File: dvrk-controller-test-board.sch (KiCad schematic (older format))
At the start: 21 parts

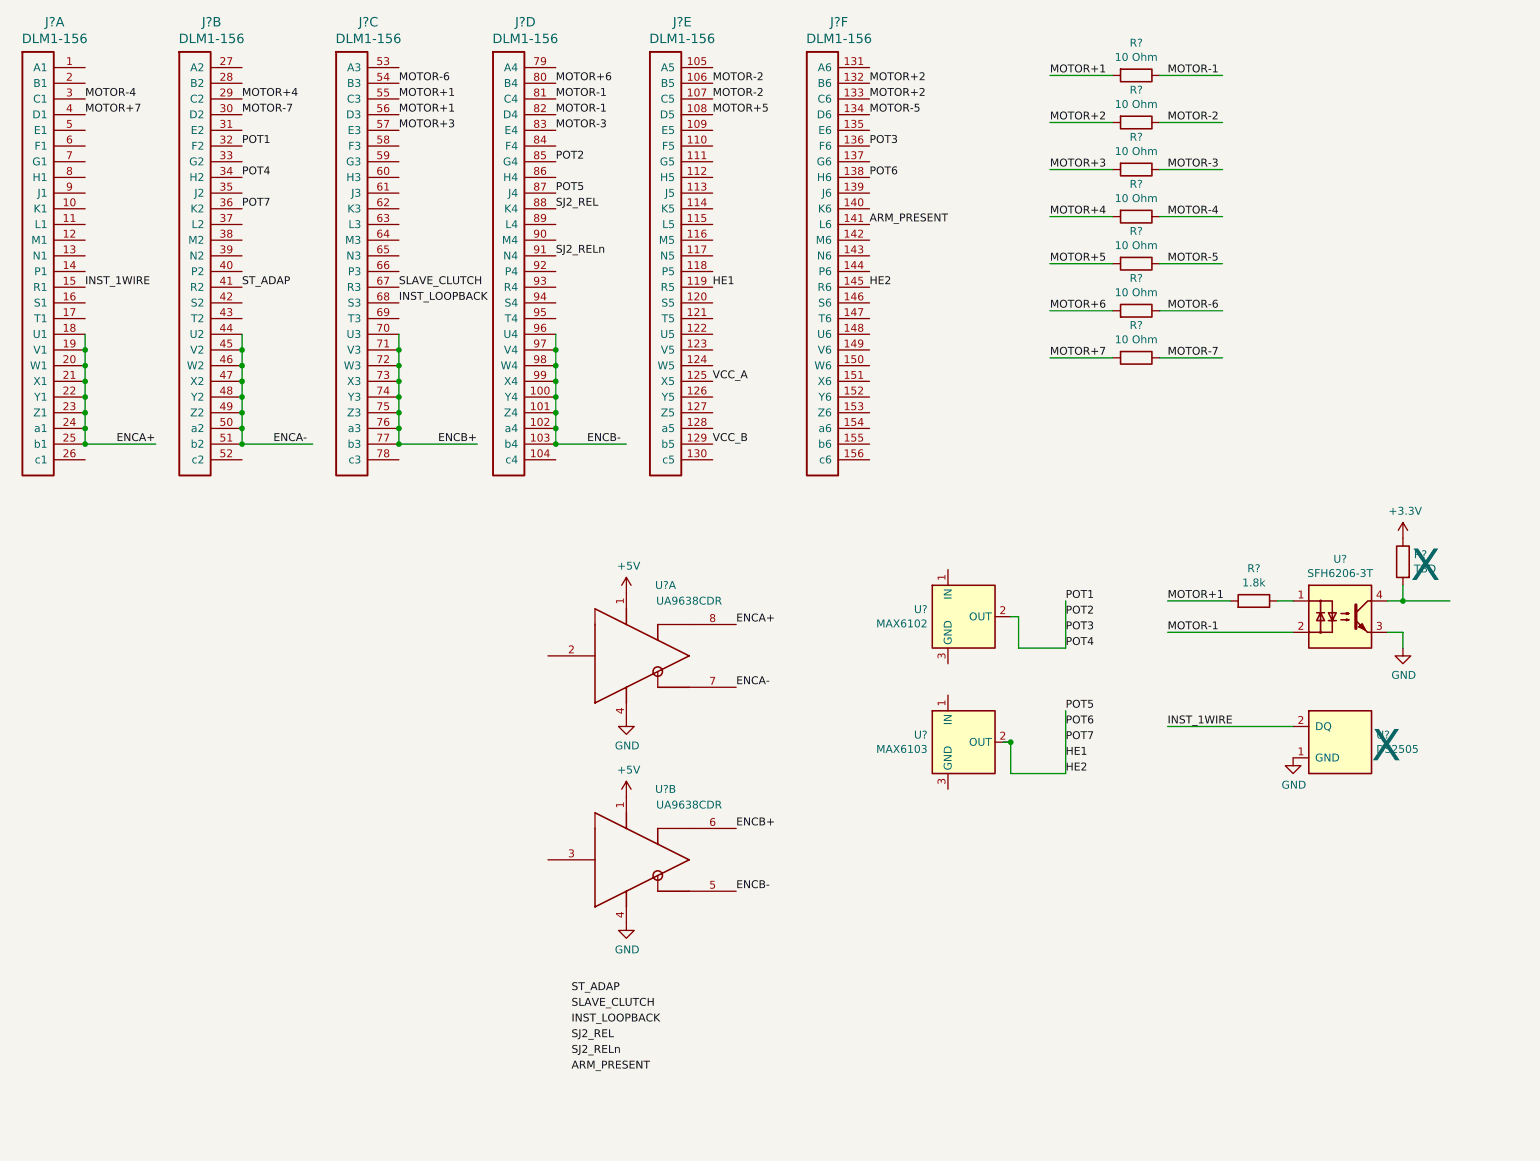
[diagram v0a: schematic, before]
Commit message: routing done. drc pass
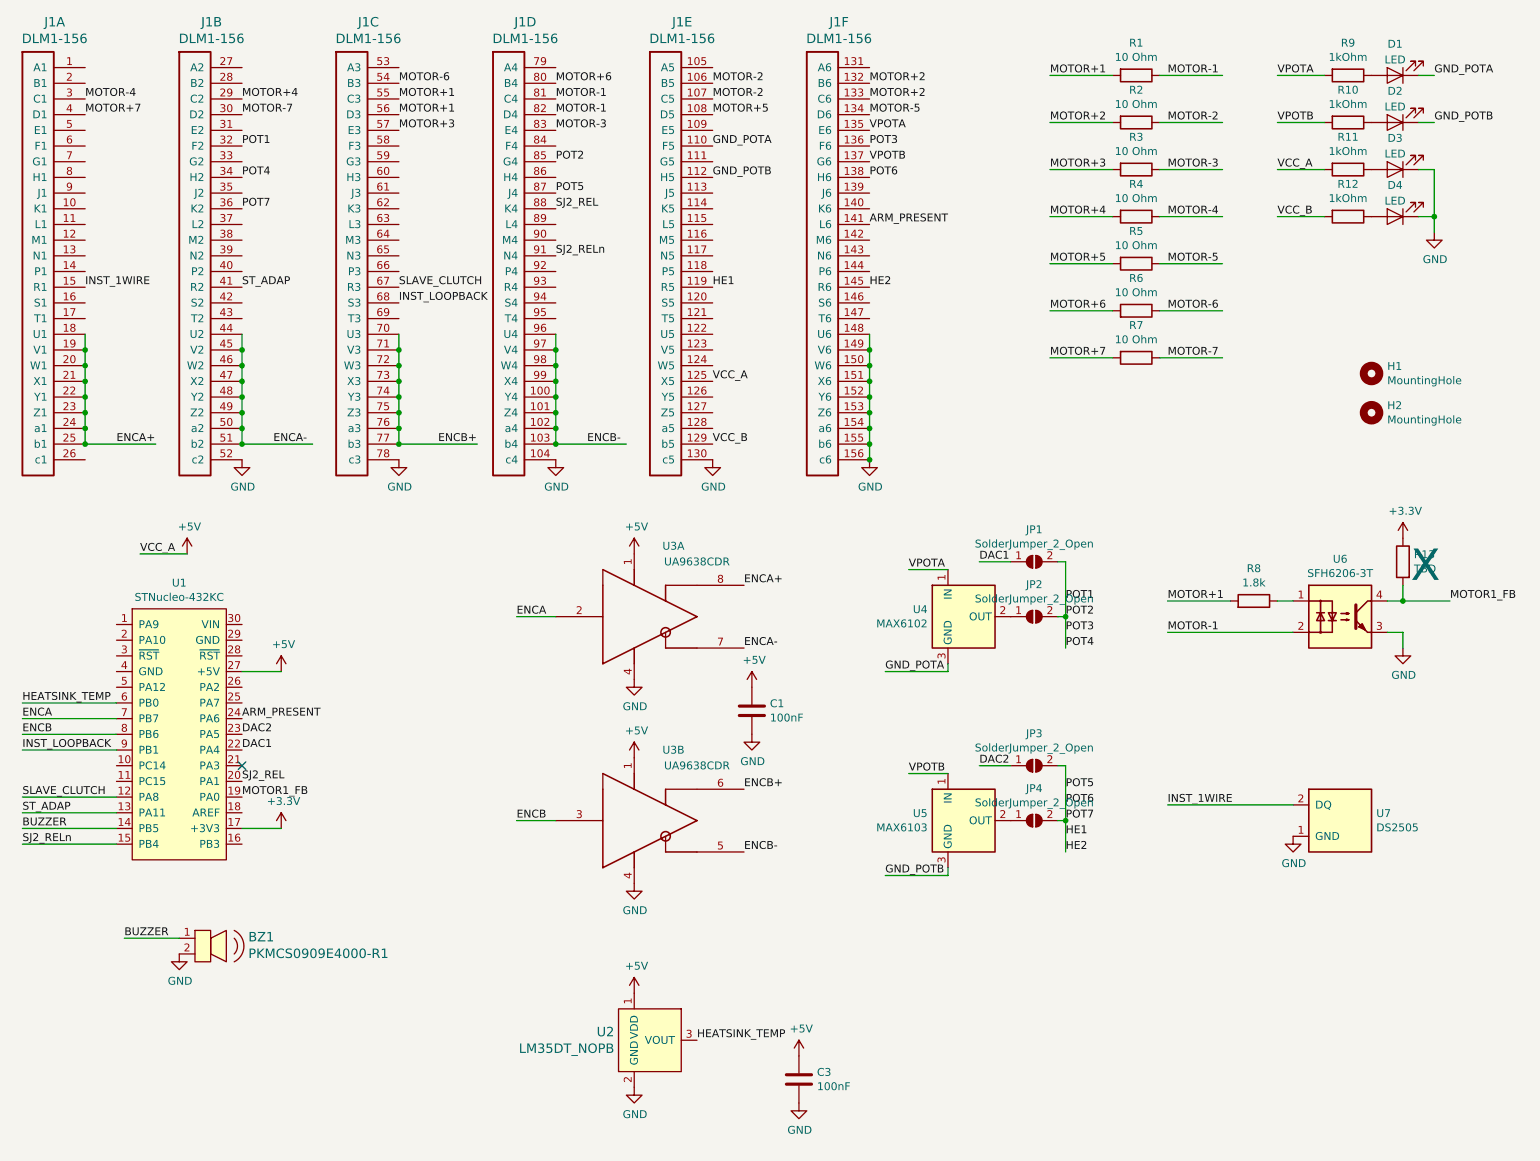
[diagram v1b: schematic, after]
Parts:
- added BZ1: PKMCS0909E4000-R1, digikey-footprints:Piezo_9x9mm_PKMCS0909E4000-R1, symbol dk_Alarms-Buzzers-and-Sirens:PKMCS0909E4000-R1
- added C1, C3: 100nF, Capacitor_SMD:C_0402_1005Metric, symbol Device:C
- added D1, D2, D3, D4: LED, LED_SMD:LED_0402_1005Metric, symbol Device:LED
- added H1, H2: MountingHole, MountingHole:MountingHole_3.2mm_M3, symbol Mechanical:MountingHole
- added JP1, JP2, JP3, JP4: SolderJumper_2_Open, Jumper:SolderJumper-2_P1.3mm_Open_TrianglePad1.0x1.5mm, symbol Jumper:SolderJumper_2_Open
- added R10, R11, R12, R9: 1kOhm, Resistor_SMD:R_0402_1005Metric, symbol Device:R
- added U1: STNucleo-432KC, dvrk:STNucleo32, symbol dvrk:STNucleo-432KC
- added U2: LM35DT_NOPB, Package_TO_SOT_THT:TO-220-3_Vertical, symbol dk_Temperature-Sensors-Analog-and-Digital-Output:LM35DT_NOPB
- J1: renamed from J?; footprint (none) -> dvrk:DLM1-Plug
- R1, R2, R3, R4, R5, R6, R7: renamed from R?; footprint (none) -> Package_TO_SOT_THT:TO-220-2_Vertical
- R13, R8: renamed from R?; footprint (none) -> Resistor_SMD:R_0402_1005Metric
- U7: renamed from U?; footprint (none) -> dvrk:TSOC-6
- gave numbers to parts that had none: 4
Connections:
- net labels added: BUZZER, DAC1, DAC2, ENCA, ENCB, GND_POTA, GND_POTB, HEATSINK_TEMP, MOTOR1_FB, VPOTA, VPOTB
- wire segments 63 -> 103
- no-connect marks 0 -> 1
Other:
- moved on the sheet: U3A, U3B, U5, U7

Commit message: added logo
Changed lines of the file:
@@
+	1    0    0    -1
+$EndComp
+$Comp
+L dvrk-logo:LOGO #G?
+U 1 1 5C5392A2
+P 6550 7050
+F 0 "#G?" H 6550 6947 60  0001 C CNN
+F 1 "LOGO" H 6550 7153 60  0001 C CNN
+F 2 "dvrk:dvrk-logo" H 6550 7050 50  0001 C CNN
+F 3 "" H 6550 7050 50  0001 C CNN
+	1    6550 7050
 	1    0    0    -1
 $EndComp

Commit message: reannotate
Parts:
- renumbered C3 to C2
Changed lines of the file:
@@
 	9100 4700 8300 4700
 $Comp
-L power:GND #PWR0101
+L power:GND #PWR022
 U 1 1 5C3598A0
 P 9800 4800
-F 0 "#PWR0101" H 9800 4550 50  0001 C CNN
+F 0 "#PWR022" H 9800 4550 50  0001 C CNN
 F 1 "GND" H 9805 4627 50  0000 C CNN
 F 2 "" H 9800 4800 50  0001 C CNN
@@
 	9800 4500 9800 4400
 $Comp
-L power:+3.3V #PWR0102
+L power:+3.3V #PWR021
 U 1 1 5C360C60
 P 9800 4100
-F 0 "#PWR0102" H 9800 3950 50  0001 C CNN
+F 0 "#PWR021" H 9800 3950 50  0001 C CNN
 F 1 "+3.3V" H 9815 4273 50  0000 C CNN
 F 2 "" H 9800 4100 50  0001 C CNN
@@
 	9100 5800 8300 5800
 $Comp
-L power:GND #PWR0103
+L power:GND #PWR020
 U 1 1 5C3C0652
 P 9100 6000
-F 0 "#PWR0103" H 9100 5750 50  0001 C CNN
+F 0 "#PWR020" H 9100 5750 50  0001 C CNN
 F 1 "GND" H 9105 5827 50  0000 C CNN
 F 2 "" H 9100 6000 50  0001 C CNN
@@
 ENCB-
 $Comp
-L power:GND #PWR0104
+L power:GND #PWR09
 U 1 1 5C3F2BBE
 P 4900 5000
-F 0 "#PWR0104" H 4900 4750 50  0001 C CNN
+F 0 "#PWR09" H 4900 4750 50  0001 C CNN
 F 1 "GND" H 4905 4827 50  0000 C CNN
 F 2 "" H 4900 5000 50  0001 C CNN
@@
 $EndComp
 $Comp
-L power:GND #PWR0105
+L power:GND #PWR011
 U 1 1 5C3F3A4C
 P 4900 6300
-F 0 "#PWR0105" H 4900 6050 50  0001 C CNN
+F 0 "#PWR011" H 4900 6050 50  0001 C CNN
 F 1 "GND" H 4905 6127 50  0000 C CNN
 F 2 "" H 4900 6300 50  0001 C CNN
@@
 $EndComp
 $Comp
-L power:+5V #PWR0106
+L power:+5V #PWR08
 U 1 1 5C3F6B67
 P 4900 4200
-F 0 "#PWR0106" H 4900 4050 50  0001 C CNN
+F 0 "#PWR08" H 4900 4050 50  0001 C CNN
 F 1 "+5V" H 4915 4373 50  0000 C CNN
 F 2 "" H 4900 4200 50  0001 C CNN
@@
 $EndComp
 $Comp
-L power:+5V #PWR0107
+L power:+5V #PWR010
 U 1 1 5C3F716D
 P 4900 5500
-F 0 "#PWR0107" H 4900 5350 50  0001 C CNN
+F 0 "#PWR010" H 4900 5350 50  0001 C CNN
 F 1 "+5V" H 4915 5673 50  0000 C CNN
 F 2 "" H 4900 5500 50  0001 C CNN
@@
 	9900 2050 10000 2050
 $Comp
-L power:GND #PWR0108
+L power:GND #PWR023
 U 1 1 5C3426EE
 P 10000 2150
-F 0 "#PWR0108" H 10000 1900 50  0001 C CNN
+F 0 "#PWR023" H 10000 1900 50  0001 C CNN
 F 1 "GND" H 10005 1977 50  0000 C CNN
 F 2 "" H 10000 2150 50  0001 C CNN
@@
 MOTOR1_FB
 $Comp
-L power:+5V #PWR0109
+L power:+5V #PWR04
 U 1 1 5C34AC27
 P 2650 4950
-F 0 "#PWR0109" H 2650 4800 50  0001 C CNN
+F 0 "#PWR04" H 2650 4800 50  0001 C CNN
 F 1 "+5V" H 2665 5123 50  0000 C CNN
 F 2 "" H 2650 4950 50  0001 C CNN
@@
 ENCB
 $Comp
-L power:+5V #PWR06
+L power:+5V #PWR012
 U 1 1 5C35BBD3
 P 4900 7000
-F 0 "#PWR06" H 4900 6850 50  0001 C CNN
+F 0 "#PWR012" H 4900 6850 50  0001 C CNN
 F 1 "+5V" H 4915 7173 50  0000 C CNN
 F 2 "" H 4900 7000 50  0001 C CNN
@@
 $EndComp
 $Comp
-L power:GND #PWR07
+L power:GND #PWR013
 U 1 1 5C35E64A
 P 4900 7600
-F 0 "#PWR07" H 4900 7350 50  0001 C CNN
+F 0 "#PWR013" H 4900 7350 50  0001 C CNN
 F 1 "GND" H 4905 7427 50  0000 C CNN
 F 2 "" H 4900 7600 50  0001 C CNN
@@
 $EndComp
 $Comp
-L power:GND #PWR010
+L power:GND #PWR016
 U 1 1 5C363C3C
 P 5650 5350
-F 0 "#PWR010" H 5650 5100 50  0001 C CNN
+F 0 "#PWR016" H 5650 5100 50  0001 C CNN
 F 1 "GND" H 5655 5177 50  0000 C CNN
 F 2 "" H 5650 5350 50  0001 C CNN
@@
 $EndComp
 $Comp
-L power:+5V #PWR09
+L power:+5V #PWR015
 U 1 1 5C363595
 P 5650 5050
-F 0 "#PWR09" H 5650 4900 50  0001 C CNN
+F 0 "#PWR015" H 5650 4900 50  0001 C CNN
 F 1 "+5V" H 5665 5223 50  0000 C CNN
 F 2 "" H 5650 5050 50  0001 C CNN
@@
 $EndComp
 $Comp
-L Device:C C3
+L Device:C C2
 U 1 1 5C39201B
 P 5950 7550
-F 0 "C3" H 6065 7596 50  0000 L CNN
+F 0 "C2" H 6065 7596 50  0000 L CNN
 F 1 "100nF" H 6065 7505 50  0000 L CNN
 F 2 "Capacitor_SMD:C_0402_1005Metric" H 5988 7400 50  0001 C CNN
@@
 $EndComp
 $Comp
-L power:GND #PWR014
+L power:GND #PWR018
 U 1 1 5C392021
 P 5950 7700
-F 0 "#PWR014" H 5950 7450 50  0001 C CNN
+F 0 "#PWR018" H 5950 7450 50  0001 C CNN
 F 1 "GND" H 5955 7527 50  0000 C CNN
 F 2 "" H 5950 7700 50  0001 C CNN
@@
 $EndComp
 $Comp
-L power:+5V #PWR013
+L power:+5V #PWR017
 U 1 1 5C392027
 P 5950 7400
-F 0 "#PWR013" H 5950 7250 50  0001 C CNN
+F 0 "#PWR017" H 5950 7250 50  0001 C CNN
 F 1 "+5V" H 5965 7573 50  0000 C CNN
 F 2 "" H 5950 7400 50  0001 C CNN
@@
 	6400 3500 6400 3600
 $Comp
-L power:GND #PWR015
+L power:GND #PWR019
 U 1 1 5C3AEDB9
 P 6400 3600
-F 0 "#PWR015" H 6400 3350 50  0001 C CNN
+F 0 "#PWR019" H 6400 3350 50  0001 C CNN
 F 1 "GND" H 6405 3427 50  0000 C CNN
 F 2 "" H 6400 3600 50  0001 C CNN
@@
 $EndComp
 $Comp
-L power:GND #PWR08
+L power:GND #PWR014
 U 1 1 5C3AF1A8
 P 5400 3600
-F 0 "#PWR08" H 5400 3350 50  0001 C CNN
+F 0 "#PWR014" H 5400 3350 50  0001 C CNN
 F 1 "GND" H 5405 3427 50  0000 C CNN
 F 2 "" H 5400 3600 50  0001 C CNN
@@
 $EndComp
 $Comp
-L power:GND #PWR05
+L power:GND #PWR07
 U 1 1 5C3AF6B3
 P 4400 3600
-F 0 "#PWR05" H 4400 3350 50  0001 C CNN
+F 0 "#PWR07" H 4400 3350 50  0001 C CNN
 F 1 "GND" H 4405 3427 50  0000 C CNN
 F 2 "" H 4400 3600 50  0001 C CNN
@@
 Connection ~ 6400 3600
 $Comp
-L power:GND #PWR04
+L power:GND #PWR06
 U 1 1 5C3B1068
 P 3400 3600
-F 0 "#PWR04" H 3400 3350 50  0001 C CNN
+F 0 "#PWR06" H 3400 3350 50  0001 C CNN
 F 1 "GND" H 3405 3427 50  0000 C CNN
 F 2 "" H 3400 3600 50  0001 C CNN
@@
 	1750 4200 2050 4200
 $Comp
-L power:+3.3V #PWR0110
+L power:+3.3V #PWR05
 U 1 1 5C49D0FE
 P 2650 5950
-F 0 "#PWR0110" H 2650 5800 50  0001 C CNN
+F 0 "#PWR05" H 2650 5800 50  0001 C CNN
 F 1 "+3.3V" H 2665 6123 50  0000 C CNN
 F 2 "" H 2650 5950 50  0001 C CNN
@@
 $EndComp
 $Comp
-L dvrk-logo:LOGO #G?
-U 1 1 5C5392A2
-P 6550 7050
-F 0 "#G?" H 6550 6947 60  0001 C CNN
-F 1 "LOGO" H 6550 7153 60  0001 C CNN
-F 2 "dvrk:dvrk-logo" H 6550 7050 50  0001 C CNN
-F 3 "" H 6550 7050 50  0001 C CNN
-	1    6550 7050
-	1    0    0    -1
-$EndComp
+L dvrk-logo:LOGO #G1
+U 1 1 5C543589
+P 6550 7000
+F 0 "#G1" H 6550 6897 60  0001 C CNN
+F 1 "LOGO" H 6550 7103 60  0001 C CNN
+F 2 "dvrk:dvrk-logo" H 6550 7000 50  0001 C CNN
+F 3 "" H 6550 7000 50  0001 C CNN
+	1    6550 7000
+	1    0    0    -1
+$EndComp
